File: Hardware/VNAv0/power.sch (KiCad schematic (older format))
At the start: 41 parts, among them Q1 RE1C002UN, U4 LP5912, U5 LP5912, U6 MIC5366-1.8

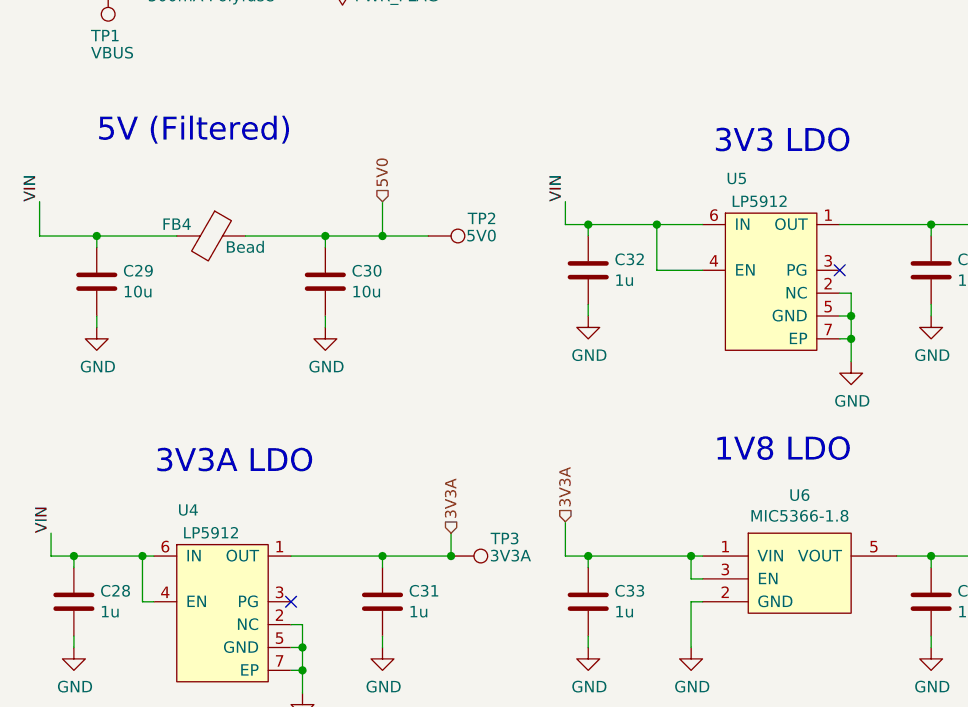
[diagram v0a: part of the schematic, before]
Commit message: tx chain now works, however output power too low
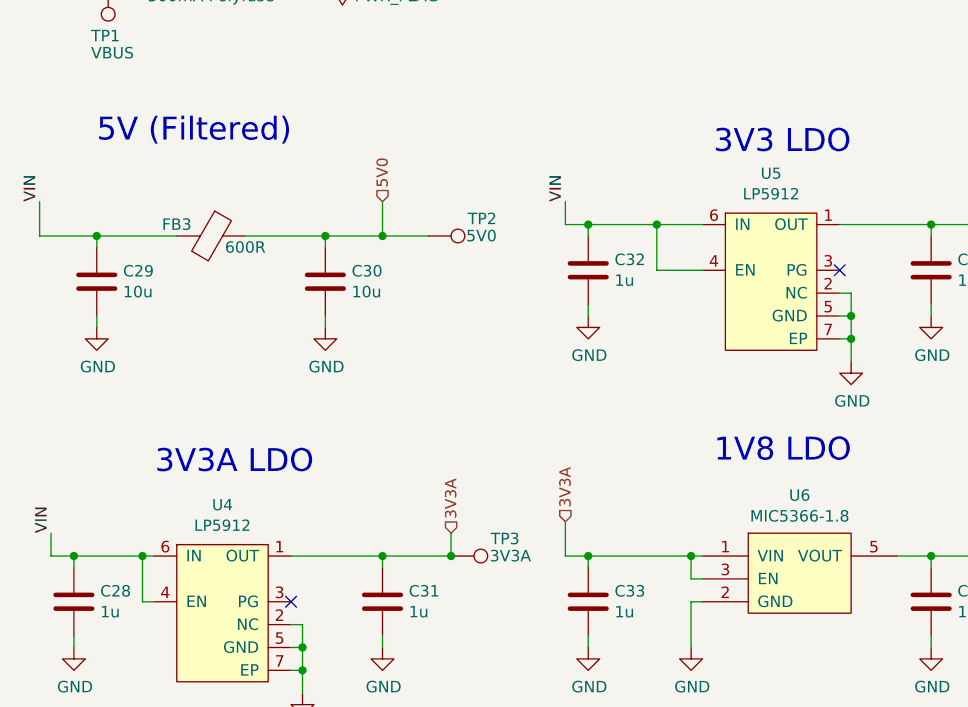
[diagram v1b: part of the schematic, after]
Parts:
- removed FB4: Bead, VNA_Footprints:BEADC1608X95N, symbol VNA_Symbols:Ferrite_Bead_PWR
- added FB3: 600R, symbol VNA_Symbols:Ferrite_Bead_PWR
- U4, U5: footprint Package_DFN_QFN:DFN-6-1EP_2x2mm_P0.65mm_EP1x1.6mm -> (none)
- U6: footprint Package_TO_SOT_SMD:SOT-353_SC-70-5 -> (none)
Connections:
- net 5V0: now also FB3.1
- net VIN: now also FB3.2
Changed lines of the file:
@@
 Wire Wire Line
 	3900 3950 3950 3950
-$Comp
-L VNA_Symbols:MIC5366-1.8 U?
-U 1 1 5CAA0ACF
-P 4350 4050
-AR Path="/5CA81007/5CAA0ACF" Ref="U?"  Part="1"
-AR Path="/5CA96610/5CAA0ACF" Ref="U6"  Part="1"
-F 0 "U6" H 4375 4415 50  0000 C CNN
-F 1 "MIC5366-1.8" H 4375 4324 50  0000 C CNN
-F 2 "Package_TO_SOT_SMD:SOT-353_SC-70-5" H 4150 4350 50  0001 C CNN
-F 3 "" H 4150 4350 50  0001 C CNN
-	1    4350 4050
-	1    0    0    -1
-$EndComp
 Wire Wire Line
 	1050 2400 1050 2550
@@
 Wire Wire Line
 	1200 4300 1200 4350
-$Comp
-L VNA_Symbols:LP5912 U4
-U 1 1 5CFAAA40
-P 1850 4200
-F 0 "U4" H 1700 4650 49  0000 C CNN
-F 1 "LP5912" H 1800 4550 49  0000 C CNN
-F 2 "Package_DFN_QFN:DFN-6-1EP_2x2mm_P0.65mm_EP1x1.6mm" H 1800 4550 49  0001 C CNN
-F 3 "" H 1800 4550 49  0001 C CNN
-	1    1850 4200
-	1    0    0    -1
-$EndComp
 Wire Wire Line
 	2150 4250 2200 4250
@@
 	1    0    0    -1
 $EndComp
-$Comp
-L VNA_Symbols:Ferrite_Bead_PWR FB?
-U 1 1 5CC68484
-P 1800 2550
-AR Path="/5CC68484" Ref="FB?"  Part="1"
-AR Path="/5CA96610/5CC68484" Ref="FB4"  Part="1"
-F 0 "FB4" V 1750 2400 50  0000 C CNN
-F 1 "Bead" V 1850 2700 50  0000 C CNN
-F 2 "VNA_Footprints:BEADC1608X95N" V 1730 2550 50  0001 C CNN
-F 3 "~" H 1800 2550 50  0001 C CNN
-	1    1800 2550
-	0    1    1    0
-$EndComp
-$Comp
-L VNA_Symbols:LP5912 U5
-U 1 1 5CAEAD8A
-P 4250 2750
-F 0 "U5" H 4100 3200 49  0000 C CNN
-F 1 "LP5912" H 4200 3100 49  0000 C CNN
-F 2 "Package_DFN_QFN:DFN-6-1EP_2x2mm_P0.65mm_EP1x1.6mm" H 4200 3100 49  0001 C CNN
-F 3 "" H 4200 3100 49  0001 C CNN
-	1    4250 2750
-	1    0    0    -1
-$EndComp
 Wire Wire Line
 	3750 2700 3950 2700
@@
 	1    0    0    -1
 $EndComp
+$Comp
+L VNA_Symbols:Ferrite_Bead_PWR FB3
+U 1 1 5D197BC8
+P 1800 2550
+F 0 "FB3" V 1750 2400 50  0000 C CNN
+F 1 "600R" V 1850 2700 50  0000 C CNN
+F 2 "" V 1730 2550 50  0001 C CNN
+F 3 "~" H 1800 2550 50  0001 C CNN
+	1    1800 2550
+	0    1    1    0
+$EndComp
+$Comp
+L VNA_Symbols:LP5912 U5
+U 1 1 5D198976
+P 4250 2750
+F 0 "U5" H 4250 3223 49  0000 C CNN
+F 1 "LP5912" H 4250 3133 49  0000 C CNN
+F 2 "" H 4200 3100 49  0001 C CNN
+F 3 "" H 4200 3100 49  0001 C CNN
+	1    4250 2750
+	1    0    0    -1
+$EndComp
+$Comp
+L VNA_Symbols:LP5912 U4
+U 1 1 5D1994DE
+P 1850 4200
+F 0 "U4" H 1850 4673 49  0000 C CNN
+F 1 "LP5912" H 1850 4583 49  0000 C CNN
+F 2 "" H 1800 4550 49  0001 C CNN
+F 3 "" H 1800 4550 49  0001 C CNN
+	1    1850 4200
+	1    0    0    -1
+$EndComp
+$Comp
+L VNA_Symbols:MIC5366-1.8 U6
+U 1 1 5D19A484
+P 4350 4050
+F 0 "U6" H 4375 4415 50  0000 C CNN
+F 1 "MIC5366-1.8" H 4375 4324 50  0000 C CNN
+F 2 "" H 4150 4350 50  0001 C CNN
+F 3 "" H 4150 4350 50  0001 C CNN
+	1    4350 4050
+	1    0    0    -1
+$EndComp
